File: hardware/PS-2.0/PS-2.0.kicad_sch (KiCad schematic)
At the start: 53 parts, among them J1 PinSocket_02x16_P2.54mm_Verti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, J2 Conn_01x05, J3 Conn_01x05, J8 Conn_01x02, J9 Conn_01x02, K1 RAYEX-L90, K2 RAYEX-L90, Q1 IRFPE50, Q2 IRFPE50, Q3 IRFPE50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

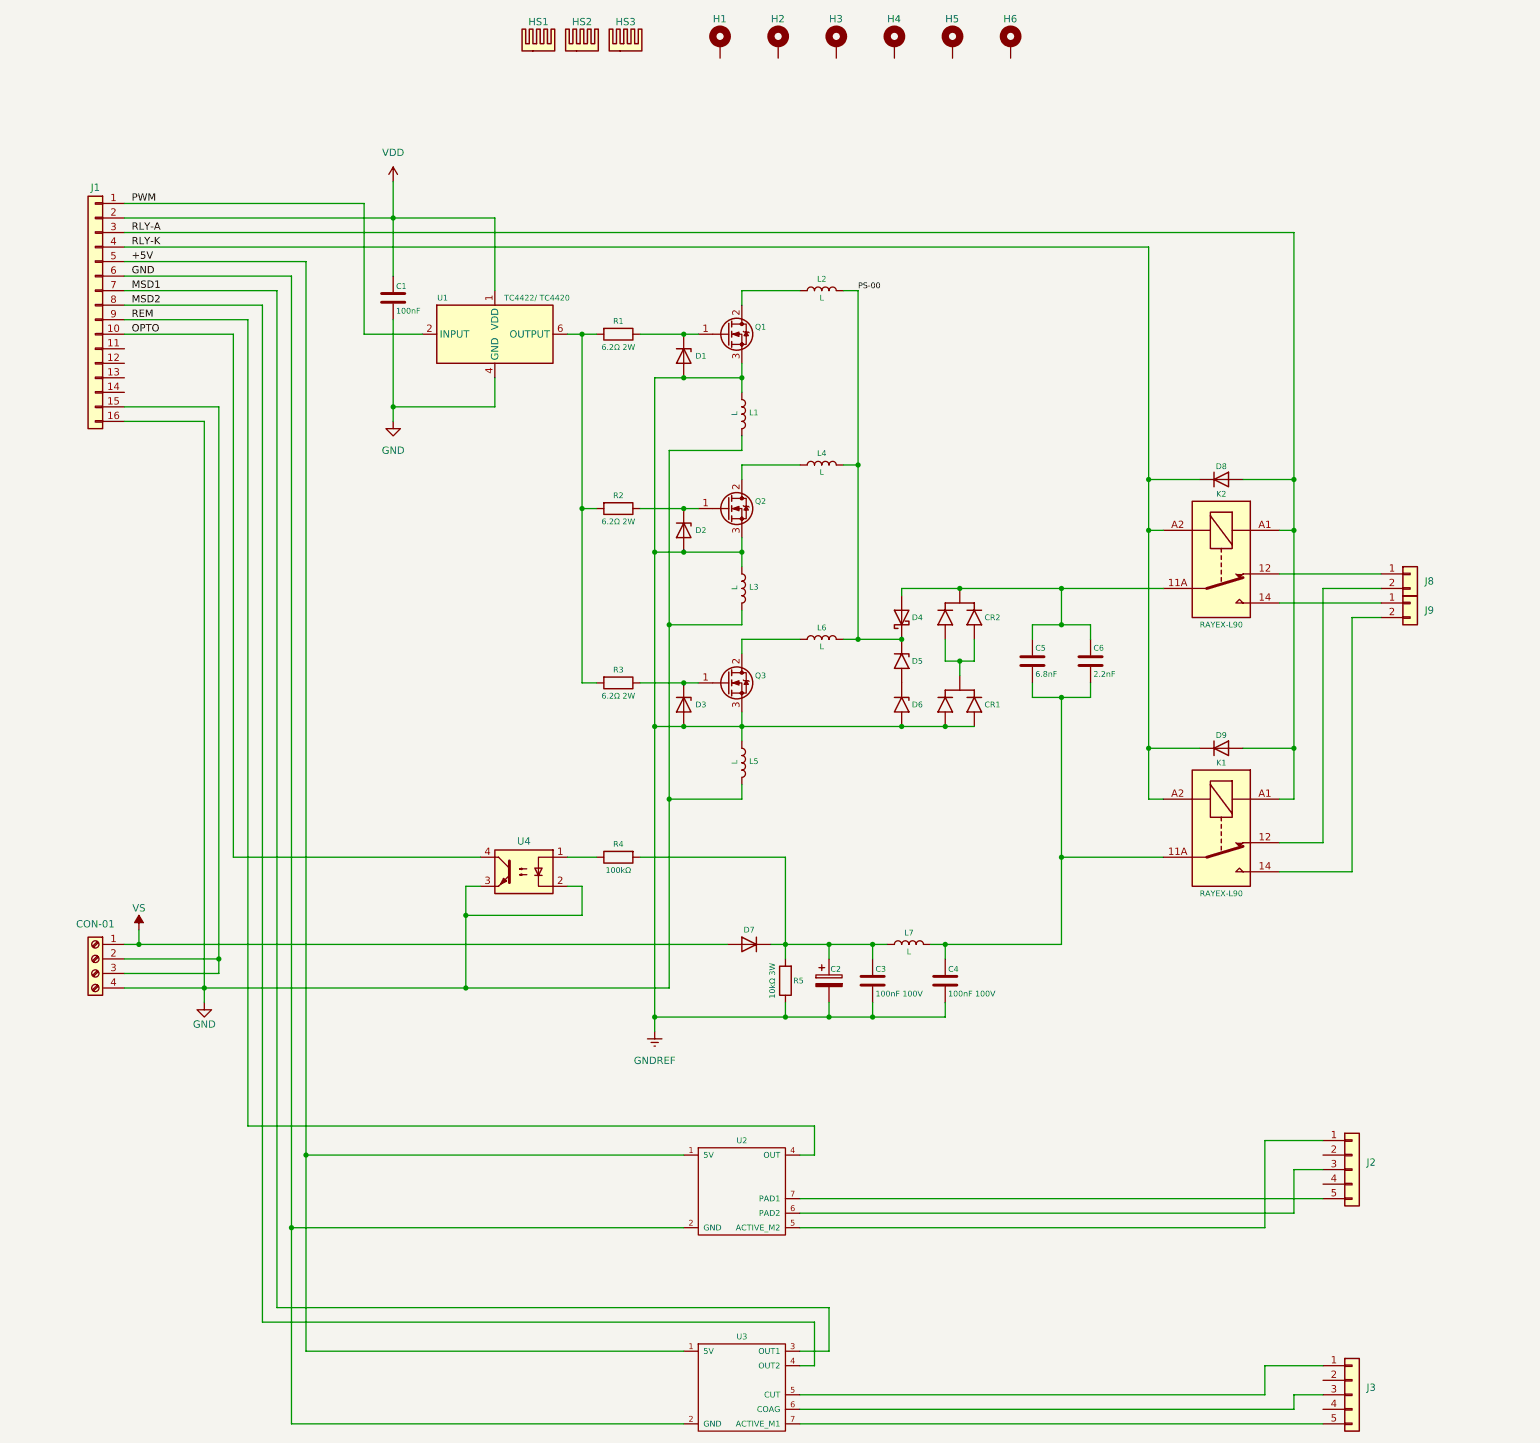
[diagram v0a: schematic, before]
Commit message: deleted:    hardware/CTL-1.0/CTL-1.0-backups/CTL-1.0-2025-06-04_115049.zip 	deleted:    hardware/CTL-1.0/CTL-1.0-backups/CTL-1.0-2025-06-04_132910.zip 	deleted:    hardware/CTL-1.0/CTL-1.0-backups/CTL-1.0-2025-06-05_142549.zip 	deleted:    hardware/CTL-1.0/CTL-1.0-backups/CTL-1.0-2025-06-05_143053.zip 	deleted:    hardware/CTL-1.0/CTL-1.0-backups/CTL-1.0-2025-06-05_144242.zip 	new file:   hardware/CTL-1.0/CTL-1.0-backups/CTL-1.0-2025-08-01_111317.zip 	new file:   hardware/CTL-1.0/CTL-1.0-backups/CTL-1.0-2025-08-01_113544.zip 	new file:   hardware/CTL-1.0/CTL-1.0-backups/CTL-1.0-2025-08-01_114559.zip 	new file:   hardware/CTL-1.0/CTL-1.0-backups/CTL-1.0-2025-08-01_115359.zip 	new file:   hardware/CTL-1.0/CTL-1.0-backups/CTL-1.0-2025-08-01_115915.zip 	new file:   hardware/CTL-1.0/CTL-1.0-backups/CTL-1.0-2025-08-01_131607.zip 	modified:   hardware/CTL-1.0/CTL-1.0.kicad_pcb 	modified:   hardware/CTL-1.0/CTL-1.0.kicad_sch 	renamed:    hardware/CTL-1.0/CTL-1.0-backups/CTL-1.0-2025-06-05_144757.zip -> hardware/CTL-1.2/CTL-1.0-backups/CTL-1.0-2025-06-05_145506.zip 	new file:   hardware/CTL-1.2/CTL-1.0-backups/CTL-1.0-2025-06-10_100335.zip 	new file:   hardware/CTL-1.2/CTL-1.0-backups/CTL-1.0-2025-06-12_095314.zip 	new file:   hardware/CTL-1.2/CTL-1.0-backups/CTL-1.0-2025-07-03_115731.zip 	new file:   hardware/CTL-1.2/CTL-1.0-backups/CTL-1.0-2025-07-16_143147.zip 	new file:   hardware/CTL-1.2/CTL-1.0-backups/CTL-1.0-2025-07-24_151142.zip 	new file:   hardware/CTL-1.2/CTL-1.0-backups/CTL-1.0-2025-07-24_172002.zip 	new file:   hardware/CTL-1.2/CTL-1.0-backups/CTL-1.0-2025-07-25_175122.zip 	new file:   hardware/CTL-1.2/CTL-1.0-backups/CTL-1.0-2025-07-26_120011.zip 	new file:   hardware/CTL-1.2/CTL-1.0-backups/CTL-1.0-2025-07-26_120808.zip 	new file:   hardware/CTL-1.2/CTL-1.0-backups/CTL-1.0-2025-07-28_094555.zip 	new file:   hardware/CTL-1.2/CTL-1.0-backups/CTL-1.0-2025-07-28_104747.zip 	new file:   hardware/CTL-1.2/CTL-1.0-backups/CTL-1.0-2025-07-28_112613.zip 	new file:   ha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
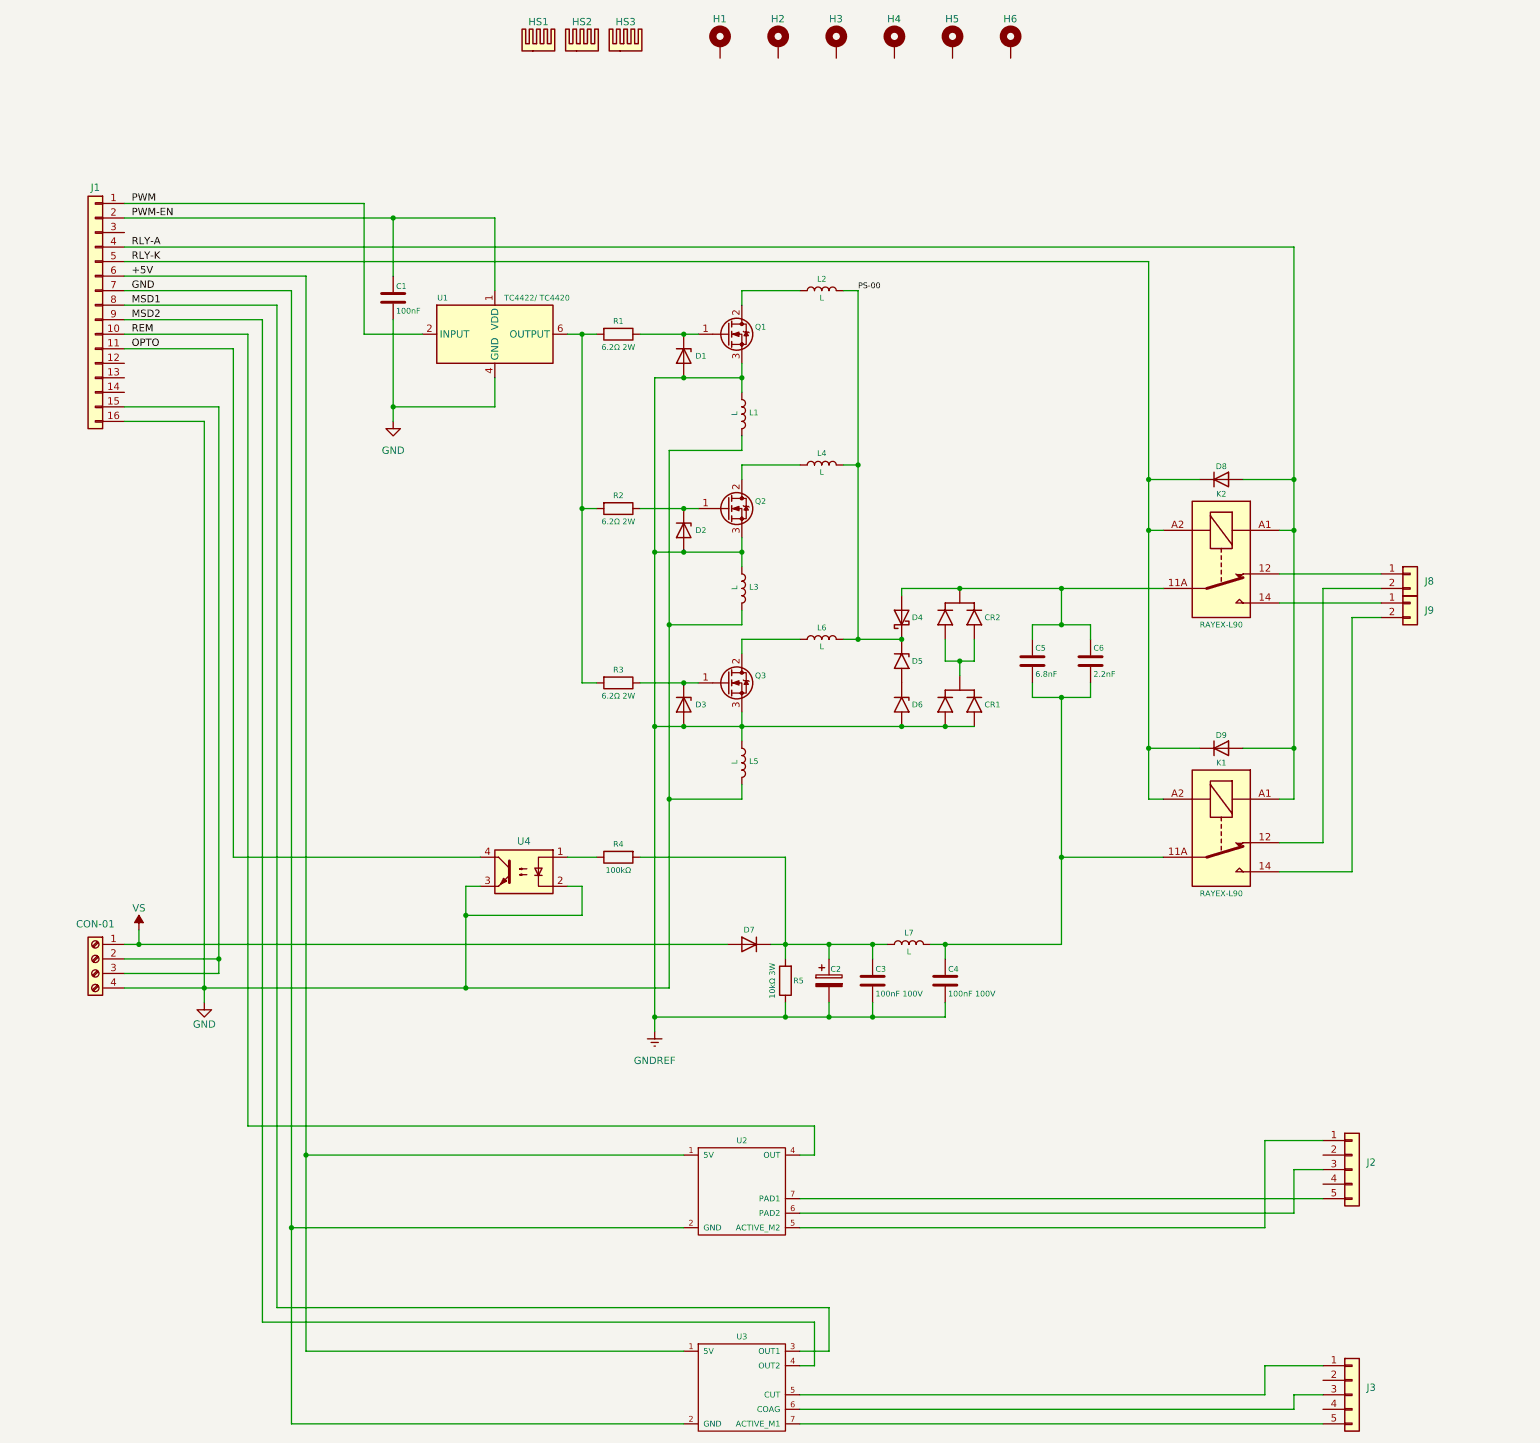
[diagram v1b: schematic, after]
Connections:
- net +5V: now also J1.6 (Pin_6); no longer J1.5 (Pin_5)
- net GND: now also J1.7 (Pin_7); no longer J1.6 (Pin_6)
- net MSD1: now also J1.8 (Pin_8); no longer J1.7 (Pin_7)
- net MSD2: now also J1.9 (Pin_9); no longer J1.8 (Pin_8)
- net OPTO: now also J1.11 (Pin_11); no longer J1.10 (Pin_10)
- net REM: now also J1.10 (Pin_10); no longer J1.9 (Pin_9)
- net RLY-A: now also J1.4 (Pin_4); no longer J1.3 (Pin_3)
- net RLY-K: now also J1.5 (Pin_5); no longer J1.4 (Pin_4)
- net VDD renamed PWM-EN

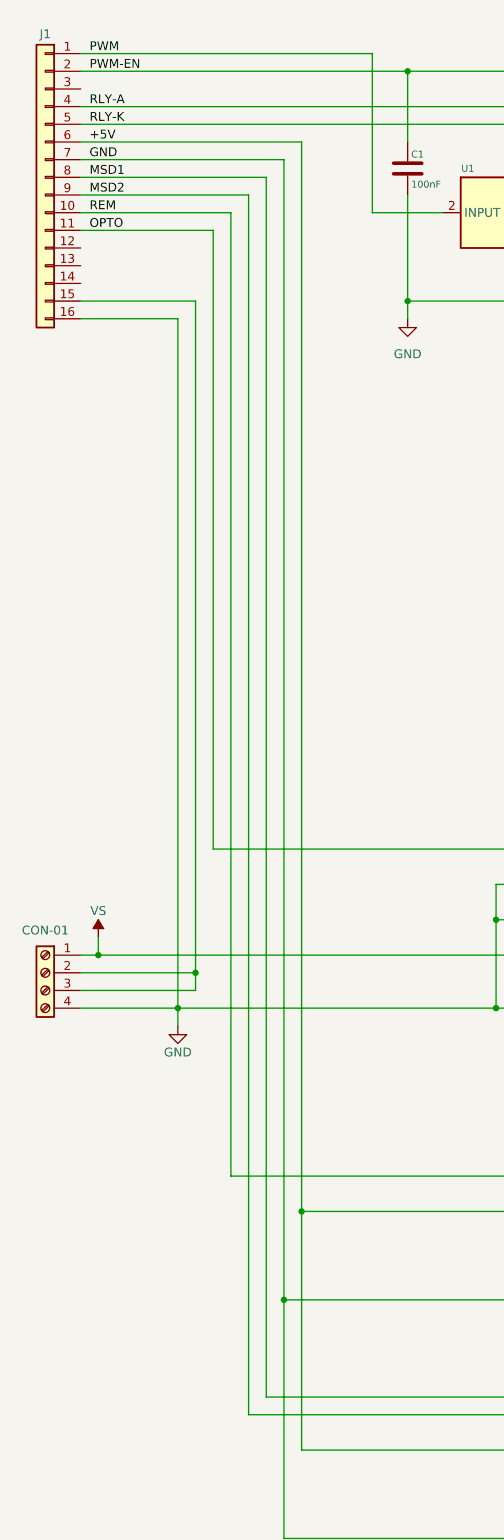
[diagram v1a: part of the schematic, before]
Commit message: modified:   .DS_Store 	deleted:    hardware/CTL-2.0/CTL-1.0-backups/CTL-1.0-2025-06-05_145506.zip 	deleted:    hardware/CTL-2.0/CTL-1.0-backups/CTL-1.0-2025-06-10_100335.zip 	deleted:    hardware/CTL-2.0/CTL-1.0-backups/CTL-1.0-2025-06-12_095314.zip 	deleted:    hardware/CTL-2.0/CTL-1.0-backups/CTL-1.0-2025-07-03_115731.zip 	deleted:    hardware/CTL-2.0/CTL-1.0-backups/CTL-1.0-2025-07-16_143147.zip 	deleted:    hardware/CTL-2.0/CTL-1.0-backups/CTL-1.0-2025-07-24_151142.zip 	deleted:    hardware/CTL-2.0/CTL-1.0-backups/CTL-1.0-2025-07-24_172002.zip 	deleted:    hardware/CTL-2.0/CTL-1.0-backups/CTL-1.0-2025-07-25_175122.zip 	deleted:    hardware/CTL-2.0/CTL-1.0-backups/CTL-1.0-2025-07-26_120011.zip 	deleted:    hardware/CTL-2.0/CTL-1.0-backups/CTL-1.0-2025-07-26_120808.zip 	deleted:    hardware/CTL-2.0/CTL-1.0-backups/CTL-1.0-2025-07-28_094555.zip 	deleted:    hardware/CTL-2.0/CTL-1.0-backups/CTL-1.0-2025-07-28_104747.zip 	deleted:    hardware/CTL-2.0/CTL-1.0-backups/CTL-1.0-2025-07-28_112613.zip 	deleted:    hardware/CTL-2.0/CTL-1.0-backups/CTL-1.0-2025-07-28_114906.zip 	deleted:    hardware/CTL-2.0/CTL-1.0-backups/CTL-1.0-2025-07-28_120848.zip 	deleted:    hardware/CTL-2.0/CTL-1.0-backups/CTL-1.0-2025-07-29_085804.zip 	deleted:    hardware/CTL-2.0/CTL-1.0-backups/CTL-1.0-2025-07-29_150437.zip 	deleted:    hardware/CTL-2.0/CTL-1.0-backups/CTL-1.0-2025-07-30_093152.zip 	deleted:    hardware/CTL-2.0/CTL-1.0-backups/CTL-1.0-2025-07-31_095618.zip 	deleted:    hardware/CTL-2.0/CTL-1.0-backups/CTL-1.0-2025-08-01_111317.zip 	deleted:    hardware/CTL-2.0/CTL-1.0-backups/CTL-1.0-2025-08-01_113544.zip 	deleted:    hardware/CTL-2.0/CTL-1.0-backups/CTL-1.0-2025-08-01_114559.zip 	deleted:    hardware/CTL-2.0/CTL-1.0-backups/CTL-1.0-2025-08-01_115359.zip 	deleted:    hardware/CTL-2.0/CTL-1.0-backups/CTL-1.0-2025-08-01_115915.zip 	deleted:    hardware/CTL-2.0/CTL-1.0-backups/CTL-1.0-2025-08-01_131607.zip 	deleted:    hardware/CTL-2.0/CTL-1.2-TopSilkscreen.png 	deleted:    hardware/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
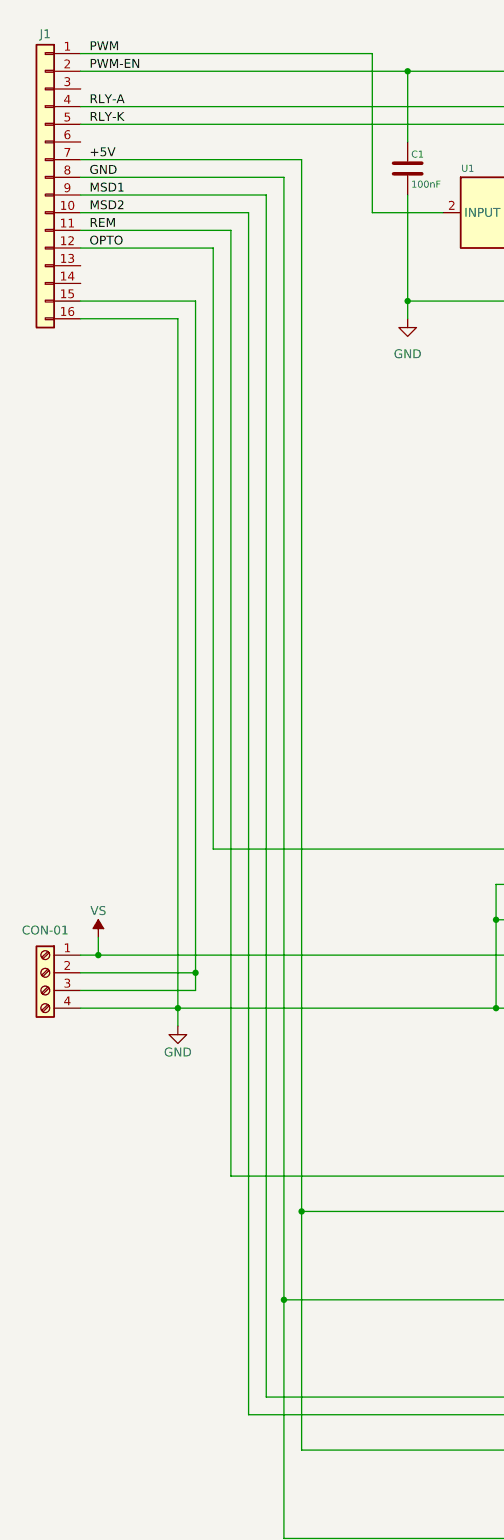
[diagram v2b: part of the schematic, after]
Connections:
- net +5V: now also J1.7 (Pin_7); no longer J1.6 (Pin_6)
- net GND: now also J1.8 (Pin_8); no longer J1.7 (Pin_7)
- net MSD1: now also J1.9 (Pin_9); no longer J1.8 (Pin_8)
- net MSD2: now also J1.10 (Pin_10); no longer J1.9 (Pin_9)
- net OPTO: now also J1.12 (Pin_12); no longer J1.11 (Pin_11)
- net REM: now also J1.11 (Pin_11); no longer J1.10 (Pin_10)
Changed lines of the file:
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@@
-	(wire
-		(pts
-			(xy 52.07 73.66) (xy 52.07 162.56)
-		)
-		(stroke
-			(width 0)
-			(type default)
-		)
-	)
 	(wire
 		(pts
@@
 	(wire
 		(pts
-			(xy 62.23 63.5) (xy 62.23 227.33)
+			(xy 62.23 66.04) (xy 62.23 227.33)
 		)
 		(stroke
@@
 	(wire
 		(pts
-			(xy 54.61 71.12) (xy 54.61 209.55)
-		)
-		(stroke
-			(width 0)
-			(type default)
-		)
-	)
-	(wire
-		(pts
 			(xy 156.21 177.8) (xy 163.83 177.8)
 		)
@@
 	(wire
 		(pts
-			(xy 59.69 66.04) (xy 59.69 241.3)
-		)
-		(stroke
-			(width 0)
-			(type default)
-		)
-	)
-	(wire
-		(pts
 			(xy 179.07 128.27) (xy 181.61 128.27)
 		)
@@
 	(wire
 		(pts
+			(xy 33.02 66.04) (xy 62.23 66.04)
+		)
+		(stroke
+			(width 0)
+			(type default)
+		)
+	)
+	(wire
+		(pts
 			(xy 52.07 162.56) (xy 95.25 162.56)
 		)
@@
 	(wire
 		(pts
-			(xy 33.02 66.04) (xy 59.69 66.04)
-		)
-		(stroke
-			(width 0)
-			(type default)
-		)
-	)
-	(wire
-		(pts
 			(xy 176.53 124.46) (xy 176.53 128.27)
 		)
@@
 	(wire
 		(pts
+			(xy 52.07 76.2) (xy 52.07 162.56)
+		)
+		(stroke
+			(width 0)
+			(type default)
+		)
+	)
+	(wire
+		(pts
 			(xy 125.73 109.22) (xy 125.73 139.7)
 		)
@@
 	(wire
 		(pts
+			(xy 59.69 68.58) (xy 59.69 241.3)
+		)
+		(stroke
+			(width 0)
+			(type default)
+		)
+	)
+	(wire
+		(pts
 			(xy 146.05 177.8) (xy 148.59 177.8)
 		)
@@
 	(wire
 		(pts
-			(xy 57.15 68.58) (xy 57.15 243.84)
-		)
-		(stroke
-			(width 0)
-			(type default)
-		)
-	)
-	(wire
-		(pts
 			(xy 237.49 105.41) (xy 237.49 143.51)
 		)
@@
 	(wire
 		(pts
+			(xy 33.02 71.12) (xy 57.15 71.12)
+		)
+		(stroke
+			(width 0)
+			(type default)
+		)
+	)
+	(wire
+		(pts
+			(xy 62.23 227.33) (xy 62.23 261.62)
+		)
+		(stroke
+			(width 0)
+			(type default)
+		)
+	)
+	(wire
+		(pts
 			(xy 151.13 256.54) (xy 232.41 256.54)
 		)
@@
 	(wire
 		(pts
-			(xy 33.02 60.96) (xy 64.77 60.96)
-		)
-		(stroke
-			(width 0)
-			(type default)
-		)
-	)
-	(wire
-		(pts
 			(xy 123.19 71.12) (xy 130.81 71.12)
 		)
@@
 	(wire
 		(pts
+			(xy 33.02 68.58) (xy 59.69 68.58)
+		)
+		(stroke
+			(width 0)
+			(type default)
+		)
+	)
+	(wire
+		(pts
 			(xy 196.85 121.92) (xy 201.93 121.92)
 		)
@@
 	(wire
 		(pts
+			(xy 64.77 63.5) (xy 64.77 214.63)
+		)
+		(stroke
+			(width 0)
+			(type default)
+		)
+	)
+	(wire
+		(pts
 			(xy 123.19 162.56) (xy 148.59 162.56)
 		)
@@
 	(wire
 		(pts
-			(xy 62.23 227.33) (xy 62.23 261.62)
-		)
-		(stroke
-			(width 0)
-			(type default)
-		)
-	)
-	(wire
-		(pts
 			(xy 163.83 177.8) (xy 163.83 180.34)
 		)
@@
 	(wire
 		(pts
+			(xy 33.02 63.5) (xy 64.77 63.5)
+		)
+		(stroke
+			(width 0)
+			(type default)
+		)
+	)
+	(wire
+		(pts
 			(xy 92.71 167.64) (xy 92.71 172.72)
 		)
@@
 	(wire
 		(pts
-			(xy 33.02 73.66) (xy 52.07 73.66)
-		)
-		(stroke
-			(width 0)
-			(type default)
-		)
-	)
-	(wire
-		(pts
 			(xy 140.97 93.98) (xy 151.13 93.98)
 		)
@@
 	(wire
 		(pts
+			(xy 57.15 71.12) (xy 57.15 243.84)
+		)
+		(stroke
+			(width 0)
+			(type default)
+		)
+	)
+	(wire
+		(pts
 			(xy 64.77 248.92) (xy 130.81 248.92)
 		)
@@
 	(wire
 		(pts
-			(xy 64.77 60.96) (xy 64.77 214.63)
-		)
-		(stroke
-			(width 0)
-			(type default)
-		)
-	)
-	(wire
-		(pts
 			(xy 156.21 187.96) (xy 156.21 190.5)
 		)
@@
 	(wire
 		(pts
+			(xy 33.02 73.66) (xy 54.61 73.66)
+		)
+		(stroke
+			(width 0)
+			(type default)
+		)
+	)
+	(wire
+		(pts
 			(xy 110.49 71.12) (xy 113.03 71.12)
 		)
@@
 	(wire
 		(pts
-			(xy 33.02 63.5) (xy 62.23 63.5)
-		)
-		(stroke
-			(width 0)
-			(type default)
-		)
-	)
-	(wire
-		(pts
 			(xy 242.57 217.17) (xy 237.49 217.17)
 		)
@@
 	(wire
 		(pts
+			(xy 54.61 73.66) (xy 54.61 209.55)
+		)
+		(stroke
+			(width 0)
+			(type default)
+		)
+	)
+	(wire
+		(pts
 			(xy 156.21 241.3) (xy 156.21 248.92)
 		)
@@
 	(wire
 		(pts
-			(xy 33.02 68.58) (xy 57.15 68.58)
-		)
-		(stroke
-			(width 0)
-			(type default)
-		)
-	)
-	(wire
-		(pts
 			(xy 113.03 71.12) (xy 115.57 71.12)
 		)
@@
 	(wire
 		(pts
+			(xy 33.02 76.2) (xy 52.07 76.2)
+		)
+		(stroke
+			(width 0)
+			(type default)
+		)
+	)
+	(wire
+		(pts
 			(xy 128.27 121.92) (xy 128.27 152.4)
 		)
@@
 	(wire
 		(pts
-			(xy 33.02 71.12) (xy 54.61 71.12)
-		)
-		(stroke
-			(width 0)
-			(type default)
-		)
-	)
-	(wire
-		(pts
 			(xy 33.02 48.26) (xy 74.93 48.26)
 		)
@@
 			(width 0)
 			(type default)
-		)
-	)
-	(label "OPTO"
-		(at 34.29 73.66 0)
-		(fields_autoplaced yes)
-		(effects
-			(font
-				(size 1.27 1.27)
-			)
-			(justify left bottom)
-		)
-	)
-	(label "MSD1"
-		(at 34.29 66.04 0)
-		(fields_autoplaced yes)
-		(effects
-			(font
-				(size 1.27 1.27)
-			)
-			(justify left bottom)
 		)
 	)
@@
 		)
 	)
-	(label "MSD2"
-		(at 34.29 68.58 0)
-		(fields_autoplaced yes)
-		(effects
-			(font
-				(size 1.27 1.27)
-			)
-			(justify left bottom)
-		)
-	)
 	(label "RLY-K"
 		(at 34.29 58.42 0)
@@
 		)
 	)
-	(label "REM"
-		(at 34.29 71.12 0)
+	(label "GND"
+		(at 34.29 66.04 0)
 		(fields_autoplaced yes)
 		(effects
@@
 	)
 	(label "+5V"
-		(at 34.29 60.96 0)
+		(at 34.29 63.5 0)
 		(fields_autoplaced yes)
 		(effects
@@
 		)
 	)
-	(label "GND"
-		(at 34.29 63.5 0)
+	(label "MSD2"
+		(at 34.29 71.12 0)
 		(fields_autoplaced yes)
 		(effects
+			(font
+				(size 1.27 1.27)
+			)
+			(justify left bottom)
+		)
+	)
+	(label "MSD1"
+		(at 34.29 68.58 0)
+		(fields_autoplaced yes)
+		(effects
+			(font
+				(size 1.27 1.27)
+			)
+			(justify left bottom)
+		)
+	)
+	(label "REM"
+		(at 34.29 73.66 0)
+		(fields_autoplaced yes)
+		(effects
+			(font
+				(size 1.27 1.27)
+			)
+			(justify left bottom)
+		)
+	)
+	(label "OPTO"
+		(at 34.29 76.2 0)
+		(fields_autoplaced yes)
+		(effects
